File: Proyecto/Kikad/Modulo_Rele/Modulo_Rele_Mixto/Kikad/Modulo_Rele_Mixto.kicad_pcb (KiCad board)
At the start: 2 copper layers, 48.9 x 19 mm, 11 parts, among them J1 TB_1X3, J2 TB_1X3, K1 RELAY_C, Q1 BC337, U3 PC817

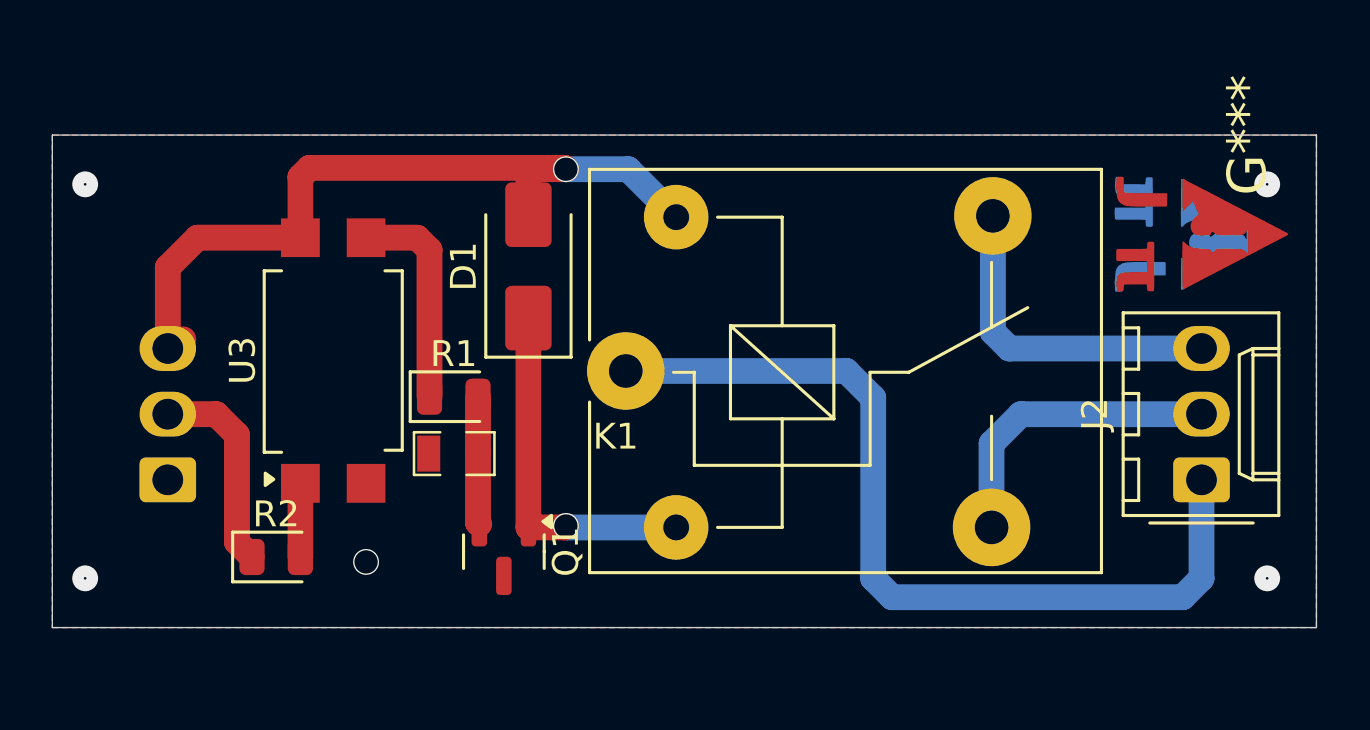
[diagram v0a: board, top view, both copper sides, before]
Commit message: hice el Rele Mixto y adjunte sus imagenes. ademas agregue la resistencia de 10K
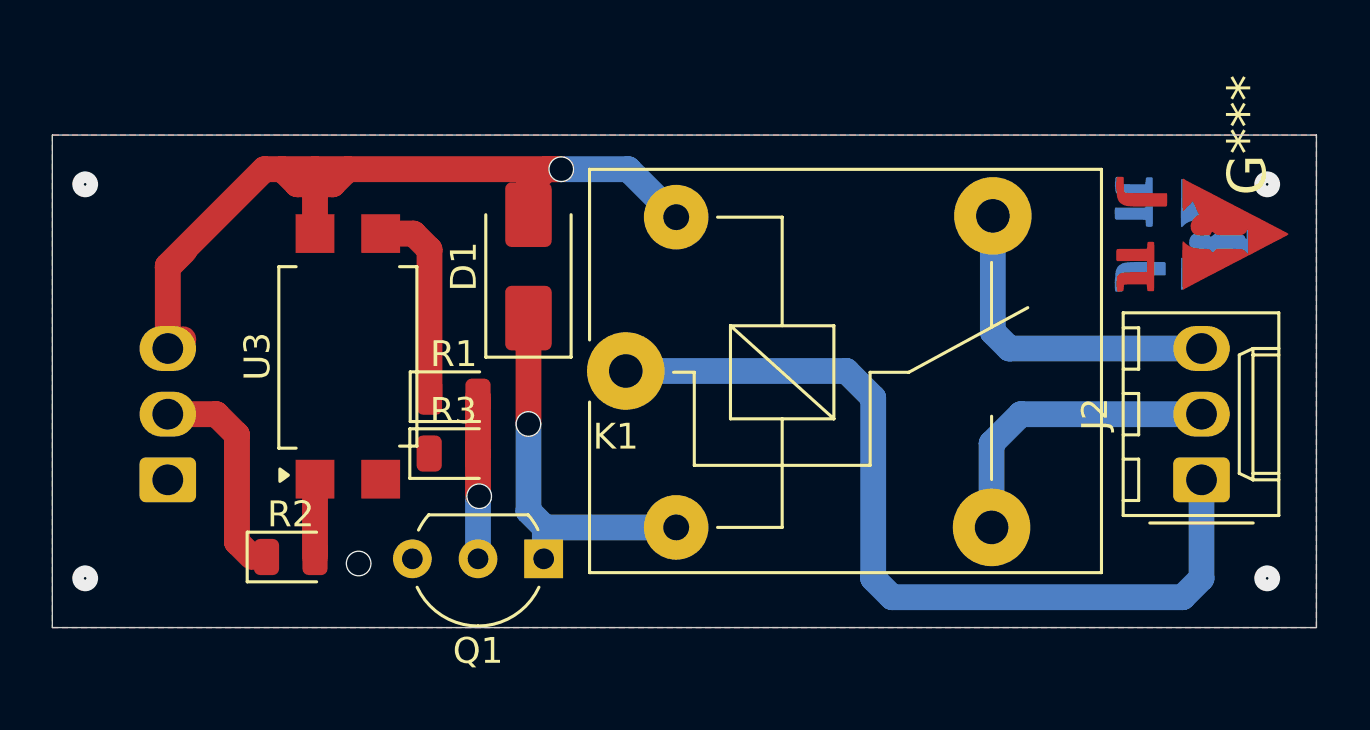
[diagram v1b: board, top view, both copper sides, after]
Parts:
- Q1: footprint Package_TO_SOT_SMD:SOT-23 -> Package_TO_SOT_THT:TO-92L_Inline_Wide
- R3: footprint EESTN5:R_0805 -> Diode_SMD:D_0805_2012Metric
- moved Q1 1.56 mm to (133.9, 123.1), turned to 180 degrees
- moved U3 0.59 mm to (126.4, 115.2)
- moved R2 0.56 mm to (124.2, 123.0)
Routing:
- net +5V: track 30.3 -> 34.7 mm
- net Net-(Q1-B): track 4.95 -> 6.24 mm, vias 0 -> 1
- net Net-(D1-A): track 13.9 -> 14.7 mm

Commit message: Agregue la carpeta Placa_Principal e hice unas correcciones en el Modulo_Rele
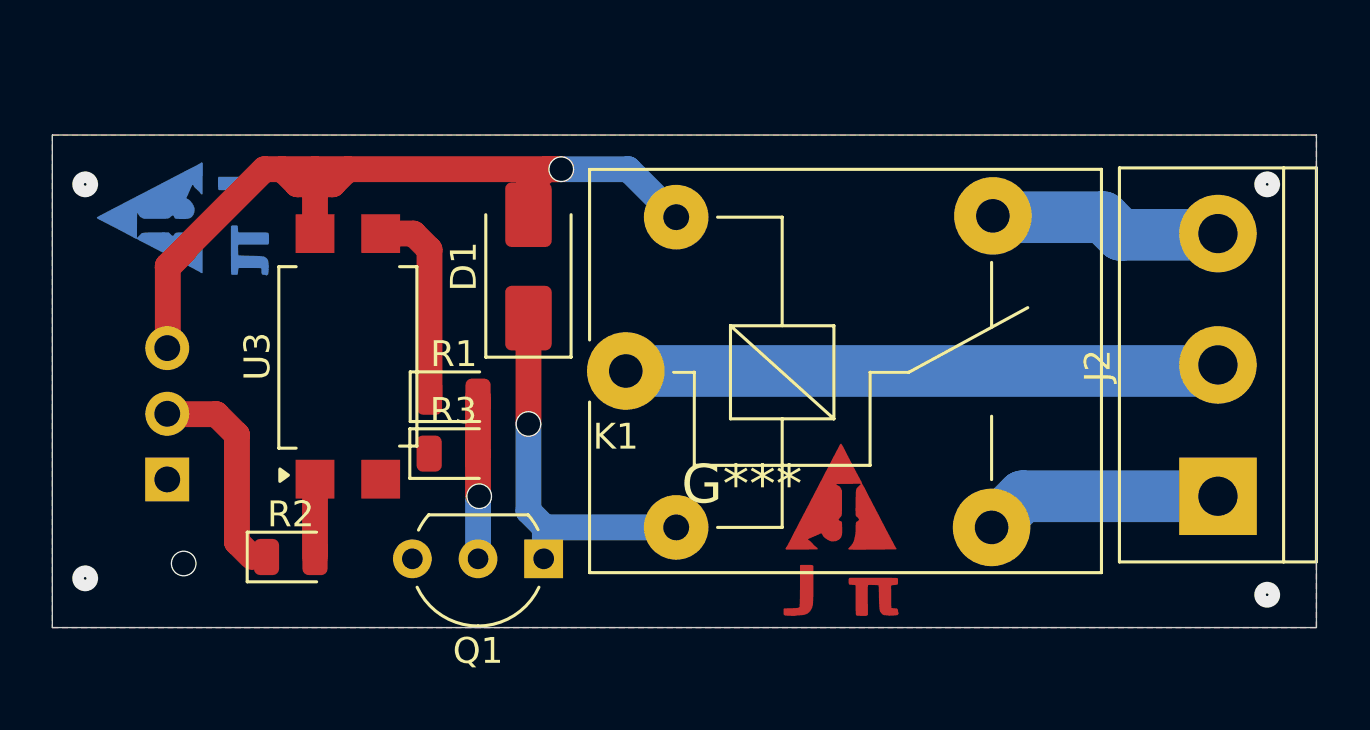
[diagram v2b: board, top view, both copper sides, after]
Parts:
- J1: footprint Connector_Molex:Molex_KK-254_AE-6410-03A_1x03_P2.54mm_Vertical -> Connector_PinHeader_2.54mm:PinHeader_1x03_P2.54mm_Vertical
- J2: footprint Connector_Molex:Molex_KK-254_AE-6410-03A_1x03_P2.54mm_Vertical -> TerminalBlock:TerminalBlock_bornier-3_P5.08mm
- moved G*** 39.3 mm to (120.0, 109.9), turned to -90 degrees
- moved G*** 18.1 mm to (145.4, 122.0), turned to 0 degrees
- moved J2 0.90 mm to (160.0, 120.7)
- turned J1 to 0 degrees
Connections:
- K1 pad 1: Net-(J2-Pad1) -> Net-(J2-Pad2)
- K1 pad 3: Net-(J2-Pad2) -> Net-(J2-Pad1)
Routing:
- net Net-(J2-Pad1): track 34.1 -> 9.25 mm
- net Net-(J2-Pad2): track 11.8 -> 23.0 mm
- net Net-(J2-Pad3): track 12.8 -> 8.99 mm
- net +5V: track 34.7 -> 34.2 mm

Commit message: Hice la Placa_Principal y corregi algunos detalles de la placa modulo rele
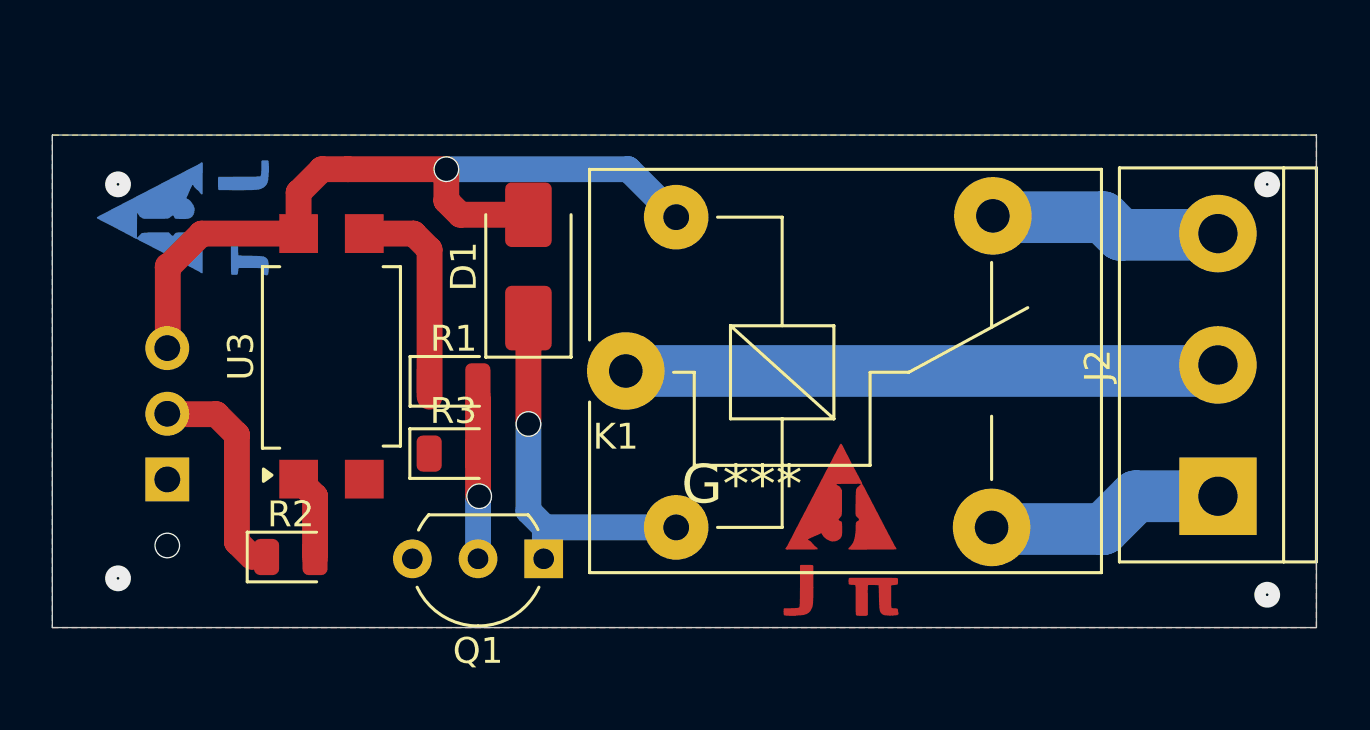
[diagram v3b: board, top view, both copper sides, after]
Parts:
- moved U3 0.63 mm to (125.7, 115.2)
- moved R1 0.60 mm to (130.5, 116.2)
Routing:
- net +5V: track 34.2 -> 30.8 mm
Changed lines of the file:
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@@
 	(footprint "Diode_SMD:D_0805_2012Metric"
 		(layer "F.Cu")
-		(at 130.4625 116.8)
+		(at 130.4567 116.205)
 		(descr "Diode SMD 0805 (2012 Metric), square (rectangular) end terminal, IPC_7351 nominal, (Body size source: https://docs.google.com/spreadsheets/d/1BsfQQcO9C6DZCsRaXUlFlo91Tg2WpOkGARC1WS5S8t0/edit?usp=sharing), generated with kicad-footprint-generator")
 		(tags "diode")
@@
 	(footprint "Package_SO:SSO-4_6.7x5.1mm_P2.54mm_Clearance8mm"
 		(layer "F.Cu")
-		(at 126.365 115.24 90)
+		(at 125.73 115.24 90)
 		(descr "4-Lead Plastic Stretched Small Outline (SSO/Stretched SO), see https://www.vishay.com/docs/84299/vor1142b4.pdf")
 		(tags "SSO Stretched SO SOIC 2.54")
@@
 	)
 	(via
-		(at 116.205 108.585)
+		(at 117.475 108.585)
 		(size 1)
 		(drill 0.1)
@@
 	)
 	(via
-		(at 116.205 123.825)
+		(at 117.475 123.825)
 		(size 1)
 		(drill 0.1)
@@
 	)
 	(segment
-		(start 134.62 108)
-		(end 126.365 108)
-		(width 1)
-		(layer "F.Cu")
-		(net 1)
-	)
-	(segment
-		(start 133.35 108.685)
-		(end 133.35 109.76)
-		(width 1)
-		(layer "F.Cu")
-		(net 1)
-	)
-	(segment
-		(start 124.41 108.585)
-		(end 123.825 108)
-		(width 1)
-		(layer "F.Cu")
-		(net 1)
-	)
-	(segment
-		(start 134.035 108)
-		(end 133.35 108.685)
-		(width 1)
-		(layer "F.Cu")
-		(net 1)
-	)
-	(segment
 		(start 119.4 111.8)
 		(end 119.4 114.935)
@@
 	)
 	(segment
-		(start 123.825 108)
-		(end 123.14 108)
+		(start 126.365 108)
+		(end 130.175 108)
 		(width 1)
 		(layer "F.Cu")
@@
 	)
 	(segment
-		(start 125.095 108.585)
-		(end 124.41 108.585)
+		(start 130.715 109.76)
+		(end 133.35 109.76)
 		(width 1)
 		(layer "F.Cu")
@@
 	)
 	(segment
-		(start 125.095 108.585)
-		(end 125.78 108.585)
+		(start 130.175 109.22)
+		(end 130.715 109.76)
 		(width 1)
 		(layer "F.Cu")
@@
 	)
 	(segment
-		(start 123.14 108)
-		(end 119.4 111.74)
+		(start 120.71 110.49)
+		(end 119.4 111.8)
 		(width 1)
 		(layer "F.Cu")
@@
 	)
 	(segment
-		(start 134.62 108)
-		(end 134.035 108)
+		(start 125.3625 108)
+		(end 126.365 108)
 		(width 1)
 		(layer "F.Cu")
@@
 	)
 	(segment
-		(start 125.095 110.49)
-		(end 125.095 108.585)
+		(start 124.46 108.9025)
+		(end 125.3625 108)
 		(width 1)
 		(layer "F.Cu")
@@
 	)
 	(segment
-		(start 120.045 111.155)
-		(end 119.4 111.8)
+		(start 130.175 108)
+		(end 130.175 109.22)
 		(width 1)
 		(layer "F.Cu")
@@
 	)
 	(segment
-		(start 125.095 108)
-		(end 123.825 108)
-		(width 1)
-		(layer "F.Cu")
-		(net 1)
-	)
-	(segment
-		(start 125.095 108.585)
-		(end 125.095 108)
-		(width 1)
-		(layer "F.Cu")
-		(net 1)
-	)
-	(segment
-		(start 126.365 108)
-		(end 125.095 108)
-		(width 1)
-		(layer "F.Cu")
-		(net 1)
-	)
-	(segment
-		(start 125.78 108.585)
-		(end 126.365 108)
+		(start 124.46 110.49)
+		(end 120.71 110.49)
 		(width 1)
 		(layer "F.Cu")
@@
 		(net 1)
 	)
+	(segment
+		(start 124.46 110.49)
+		(end 124.46 108.9025)
+		(width 1)
+		(layer "F.Cu")
+		(net 1)
+	)
 	(via
-		(at 134.62 108)
+		(at 130.175 108)
 		(size 1)
 		(drill 0.9)
@@
 	)
 	(segment
+		(start 130.175 108)
+		(end 137.21 108)
+		(width 1)
+		(layer "B.Cu")
+		(net 1)
+	)
+	(segment
 		(start 137.21 108)
 		(end 139.065 109.855)
-		(width 1)
-		(layer "B.Cu")
-		(net 1)
-	)
-	(segment
-		(start 134.62 108)
-		(end 137.21 108)
 		(width 1)
 		(layer "B.Cu")
@@
 	)
 	(via
-		(at 120.015 123.251532)
+		(at 119.38 122.555)
 		(size 1)
 		(drill 0.9)
@@
 	)
 	(segment
-		(start 152.47 120.65)
+		(start 151.265 121.855)
+		(end 151.33 121.92)
+		(width 2)
+		(layer "B.Cu")
+		(net 4)
+	)
+	(segment
+		(start 155.575 121.92)
+		(end 156.845 120.65)
+		(width 2)
+		(layer "B.Cu")
+		(net 4)
+	)
+	(segment
+		(start 156.845 120.65)
 		(end 160.02 120.65)
 		(width 2)
@@
 	)
 	(segment
-		(start 151.265 121.855)
-		(end 152.47 120.65)
+		(start 151.33 121.92)
+		(end 155.575 121.92)
 		(width 2)
 		(layer "B.Cu")
@@
 	)
 	(segment
-		(start 125.095 123)
-		(end 125.095 119.99)
+		(start 125.095 120.65)
+		(end 125.095 123.025)
 		(width 1)
 		(layer "F.Cu")
 		(net 9)
+	)
+	(segment
+		(start 124.46 120.015)
+		(end 125.095 120.65)
+		(width 1)
+		(layer "F.Cu")
+		(net 9)
+	)
+	(segment
+		(start 119.4 117.475)
+		(end 121.275 117.475)
+		(width 1)
+		(layer "F.Cu")
+		(net 10)
 	)
 	(segment
@@
 		(width 1)
 		(layer "F.Cu")
-		(net 10)
-	)
-	(segment
-		(start 121.275 117.475)
-		(end 119.4 117.475)
-		(width 1)
-		(layer "F.Cu")

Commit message: Arregle unas cosas de las dos placas
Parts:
- R2: value 220 -> 330
- moved G*** 28.1 mm to (145.4, 122.0), turned to 180 degrees
- moved J1 1.27 mm to (119.4, 118.7)
- moved U3 0.97 mm to (125.7, 116.2)
- moved J2 0.63 mm to (160.0, 121.3)
- moved K1 0.40 mm to (137.1, 116.2)
- moved Q1 0.06 mm to (134.0, 123.1)
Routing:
- net Net-(J1-Pad2): track 7.97 -> 10.1 mm
- net +5V: track 30.8 -> 29.5 mm
- net Net-(R1-Pad1): track 7.84 -> 6.74 mm
- net Net-(R2-Pad2): track 3.27 -> 2.31 mm
- net Net-(Q1-B): track 6.24 -> 6.87 mm, vias 1 -> 0
- net Net-(D1-A): track 14.7 -> 15.1 mm, vias 1 -> 0
